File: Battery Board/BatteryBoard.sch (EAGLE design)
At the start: 34 parts, among them IC1 TPS63060DSCT, J0 1725656, J1 1725669, J2 UJ2-MIBH2-4-SMT-TR, J3 MPTC-02-16-02-6.30-XX-X-V, J4 JSTPH2, J5 MPTC-02-04-02-6.30-XX-X-V-LC, Q1 IAUC60N04S6L030HATMA1, U0 STM32L031K4U6, U1 MCP73831T-2ATI_OT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

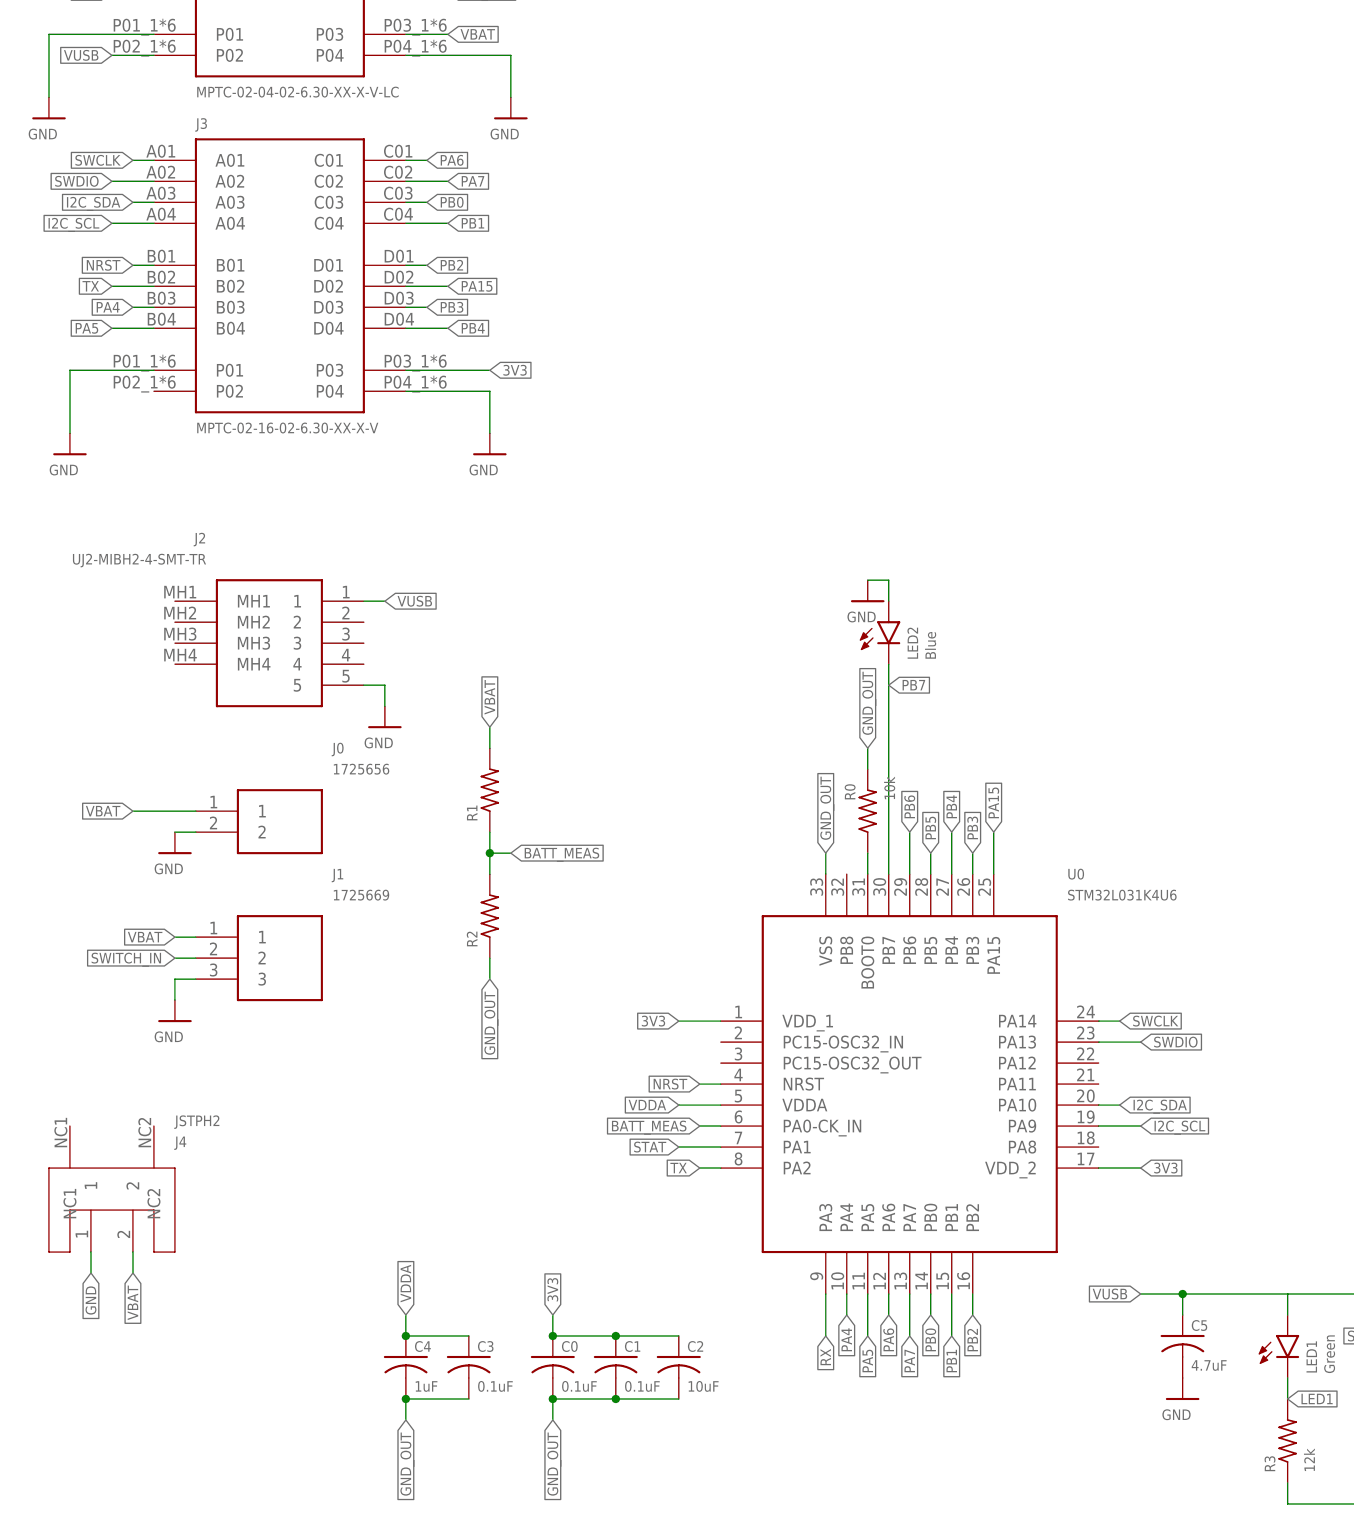
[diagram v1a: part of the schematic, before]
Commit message: Routed everything besides the pinheaders
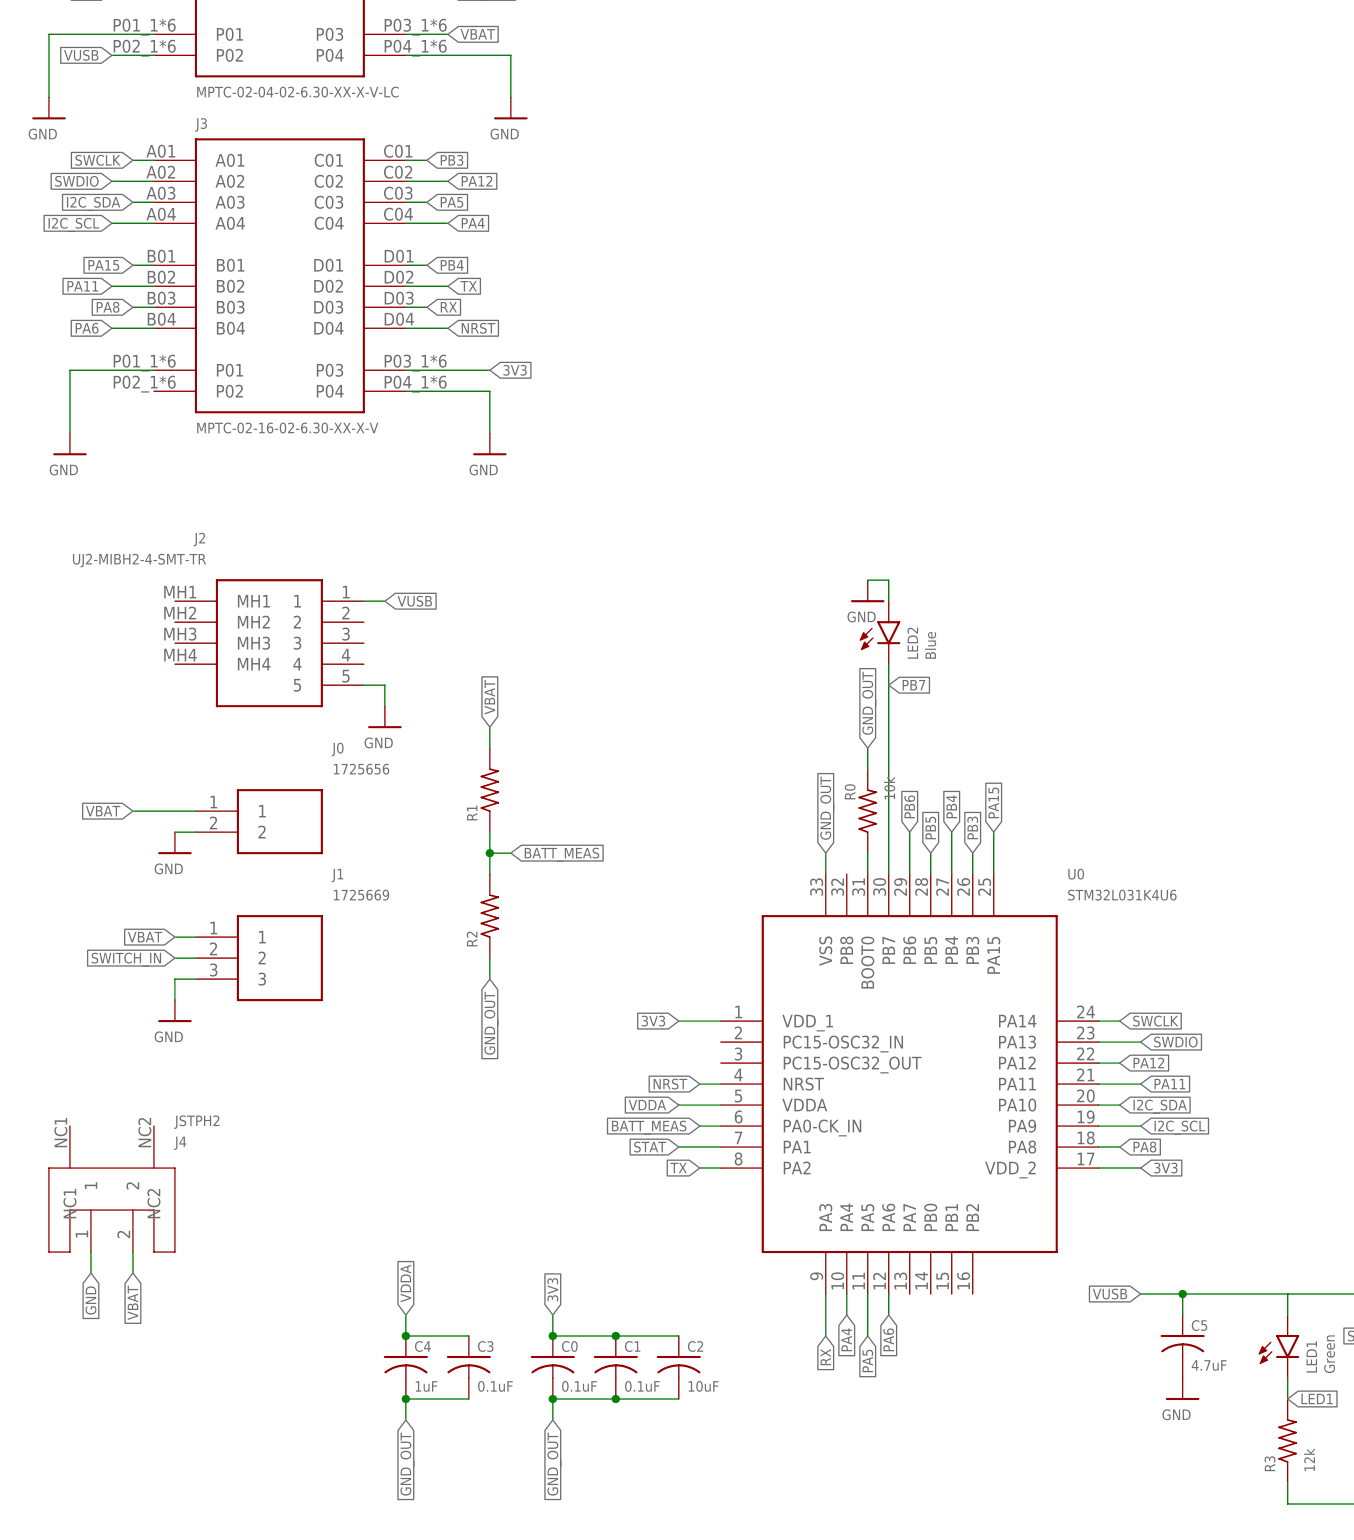
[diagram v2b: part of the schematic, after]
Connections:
- removed net PA7: J3.C02, U0.PA7
- removed net PB0: J3.C03, U0.PB0
- removed net PB1: J3.C04, U0.PB1
- removed net PB2: J3.D01, U0.PB2
- new net PA11: J3.B02, U0.PA11
- new net PA12: J3.C02, U0.PA12
- new net PA8: J3.B03, U0.PA8
- net NRST: now also J3.D04; no longer J3.B01
- net PA15: now also J3.B01; no longer J3.D02
- net PA4: now also J3.C04; no longer J3.B03
- net PA5: now also J3.C03; no longer J3.B04
- net PA6: now also J3.B04; no longer J3.C01
- net PB3: now also J3.C01; no longer J3.D03
- net PB4: now also J3.D01; no longer J3.D04
- net RX: now also J3.D03
- net TX: now also J3.D02; no longer J3.B02
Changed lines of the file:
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@@
 </segment>
 <segment>
-<pinref part="J3" gate="G$1" pin="B02"/>
-<wire x1="-53.34" y1="139.7" x2="-58.42" y2="139.7" width="0.1524" layer="91"/>
-<label x="-58.42" y="139.7" size="1.27" layer="95" rot="R180" xref="yes"/>
+<pinref part="J3" gate="G$1" pin="D02"/>
+<wire x1="-22.86" y1="139.7" x2="-17.78" y2="139.7" width="0.1524" layer="91"/>
+<label x="-17.78" y="139.7" size="1.27" layer="95" xref="yes"/>
 </segment>
 </net>
@@
 <label x="27.94" y="12.7" size="1.27" layer="95" rot="R270" xref="yes"/>
 </segment>
+<segment>
+<pinref part="J3" gate="G$1" pin="D03"/>
+<wire x1="-22.86" y1="137.16" x2="-20.32" y2="137.16" width="0.1524" layer="91"/>
+<label x="-20.32" y="137.16" size="1.27" layer="95" xref="yes"/>
+</segment>
 </net>
 <net name="NRST" class="0">
@@
 </segment>
 <segment>
-<pinref part="J3" gate="G$1" pin="B01"/>
-<wire x1="-53.34" y1="142.24" x2="-55.88" y2="142.24" width="0.1524" layer="91"/>
-<label x="-55.88" y="142.24" size="1.27" layer="95" rot="R180" xref="yes"/>
+<pinref part="J3" gate="G$1" pin="D04"/>
+<wire x1="-22.86" y1="134.62" x2="-17.78" y2="134.62" width="0.1524" layer="91"/>
+<label x="-17.78" y="134.62" size="1.27" layer="95" xref="yes"/>
 </segment>
 </net>
@@
 </segment>
 <segment>
-<pinref part="J3" gate="G$1" pin="D04"/>
-<wire x1="-22.86" y1="134.62" x2="-17.78" y2="134.62" width="0.1524" layer="91"/>
-<label x="-17.78" y="134.62" size="1.27" layer="95" xref="yes"/>
+<pinref part="J3" gate="G$1" pin="D01"/>
+<wire x1="-22.86" y1="142.24" x2="-20.32" y2="142.24" width="0.1524" layer="91"/>
+<label x="-20.32" y="142.24" size="1.27" layer="95" xref="yes"/>
 </segment>
 </net>
@@
 </segment>
 <segment>
-<pinref part="J3" gate="G$1" pin="D03"/>
-<wire x1="-22.86" y1="137.16" x2="-20.32" y2="137.16" width="0.1524" layer="91"/>
-<label x="-20.32" y="137.16" size="1.27" layer="95" xref="yes"/>
-</segment>
-</net>
-<net name="PB2" class="0">
-<segment>
-<pinref part="U0" gate="G$1" pin="PB2"/>
-<wire x1="45.72" y1="17.78" x2="45.72" y2="15.24" width="0.1524" layer="91"/>
-<label x="45.72" y="15.24" size="1.27" layer="95" rot="R270" xref="yes"/>
-</segment>
-<segment>
-<pinref part="J3" gate="G$1" pin="D01"/>
-<wire x1="-22.86" y1="142.24" x2="-20.32" y2="142.24" width="0.1524" layer="91"/>
-<label x="-20.32" y="142.24" size="1.27" layer="95" xref="yes"/>
-</segment>
-</net>
-<net name="PB1" class="0">
-<segment>
-<pinref part="U0" gate="G$1" pin="PB1"/>
-<wire x1="43.18" y1="17.78" x2="43.18" y2="12.7" width="0.1524" layer="91"/>
-<label x="43.18" y="12.7" size="1.27" layer="95" rot="R270" xref="yes"/>
+<pinref part="J3" gate="G$1" pin="C01"/>
+<wire x1="-22.86" y1="154.94" x2="-20.32" y2="154.94" width="0.1524" layer="91"/>
+<label x="-20.32" y="154.94" size="1.27" layer="95" xref="yes"/>
+</segment>
+</net>
+<net name="PA6" class="0">
+<segment>
+<pinref part="U0" gate="G$1" pin="PA6"/>
+<wire x1="35.56" y1="17.78" x2="35.56" y2="15.24" width="0.1524" layer="91"/>
+<label x="35.56" y="15.24" size="1.27" layer="95" rot="R270" xref="yes"/>
+</segment>
+<segment>
+<pinref part="J3" gate="G$1" pin="B04"/>
+<wire x1="-53.34" y1="134.62" x2="-58.42" y2="134.62" width="0.1524" layer="91"/>
+<label x="-58.42" y="134.62" size="1.27" layer="95" rot="R180" xref="yes"/>
+</segment>
+</net>
+<net name="PA5" class="0">
+<segment>
+<pinref part="U0" gate="G$1" pin="PA5"/>
+<wire x1="33.02" y1="17.78" x2="33.02" y2="12.7" width="0.1524" layer="91"/>
+<label x="33.02" y="12.7" size="1.27" layer="95" rot="R270" xref="yes"/>
+</segment>
+<segment>
+<pinref part="J3" gate="G$1" pin="C03"/>
+<wire x1="-22.86" y1="149.86" x2="-20.32" y2="149.86" width="0.1524" layer="91"/>
+<label x="-20.32" y="149.86" size="1.27" layer="95" xref="yes"/>
+</segment>
+</net>
+<net name="PA4" class="0">
+<segment>
+<pinref part="U0" gate="G$1" pin="PA4"/>
+<wire x1="30.48" y1="17.78" x2="30.48" y2="15.24" width="0.1524" layer="91"/>
+<label x="30.48" y="15.24" size="1.27" layer="95" rot="R270" xref="yes"/>
 </segment>
 <segment>
@@
 </segment>
 </net>
-<net name="PB0" class="0">
-<segment>
-<pinref part="U0" gate="G$1" pin="PB0"/>
-<wire x1="40.64" y1="17.78" x2="40.64" y2="15.24" width="0.1524" layer="91"/>
-<label x="40.64" y="15.24" size="1.27" layer="95" rot="R270" xref="yes"/>
-</segment>
-<segment>
-<pinref part="J3" gate="G$1" pin="C03"/>
-<wire x1="-22.86" y1="149.86" x2="-20.32" y2="149.86" width="0.1524" layer="91"/>
-<label x="-20.32" y="149.86" size="1.27" layer="95" xref="yes"/>
-</segment>
-</net>
-<net name="PA7" class="0">
-<segment>
-<pinref part="U0" gate="G$1" pin="PA7"/>
-<wire x1="38.1" y1="17.78" x2="38.1" y2="12.7" width="0.1524" layer="91"/>
-<label x="38.1" y="12.7" size="1.27" layer="95" rot="R270" xref="yes"/>
+<net name="PA15" class="0">
+<segment>
+<pinref part="U0" gate="G$1" pin="PA15"/>
+<wire x1="48.26" y1="68.58" x2="48.26" y2="73.66" width="0.1524" layer="91"/>
+<label x="48.26" y="73.66" size="1.27" layer="95" rot="R90" xref="yes"/>
+</segment>
+<segment>
+<pinref part="J3" gate="G$1" pin="B01"/>
+<wire x1="-53.34" y1="142.24" x2="-55.88" y2="142.24" width="0.1524" layer="91"/>
+<label x="-55.88" y="142.24" size="1.27" layer="95" rot="R180" xref="yes"/>
+</segment>
+</net>
+<net name="PA8" class="0">
+<segment>
+<pinref part="U0" gate="G$1" pin="PA8"/>
+<wire x1="60.96" y1="35.56" x2="63.5" y2="35.56" width="0.1524" layer="91"/>
+<label x="63.5" y="35.56" size="1.27" layer="95" xref="yes"/>
+</segment>
+<segment>
+<pinref part="J3" gate="G$1" pin="B03"/>
+<wire x1="-53.34" y1="137.16" x2="-55.88" y2="137.16" width="0.1524" layer="91"/>
+<label x="-55.88" y="137.16" size="1.27" layer="95" rot="R180" xref="yes"/>
+</segment>
+</net>
+<net name="PA11" class="0">
+<segment>
+<pinref part="U0" gate="G$1" pin="PA11"/>
+<wire x1="60.96" y1="43.18" x2="66.04" y2="43.18" width="0.1524" layer="91"/>
+<label x="66.04" y="43.18" size="1.27" layer="95" xref="yes"/>
+</segment>
+<segment>
+<pinref part="J3" gate="G$1" pin="B02"/>
+<wire x1="-53.34" y1="139.7" x2="-58.42" y2="139.7" width="0.1524" layer="91"/>
+<label x="-58.42" y="139.7" size="1.27" layer="95" rot="R180" xref="yes"/>
+</segment>
+</net>
+<net name="PA12" class="0">
+<segment>
+<pinref part="U0" gate="G$1" pin="PA12"/>
+<wire x1="60.96" y1="45.72" x2="63.5" y2="45.72" width="0.1524" layer="91"/>
+<label x="63.5" y="45.72" size="1.27" layer="95" xref="yes"/>
 </segment>
 <segment>
@@
 </segment>
 </net>
-<net name="PA6" class="0">
-<segment>
-<pinref part="U0" gate="G$1" pin="PA6"/>
-<wire x1="35.56" y1="17.78" x2="35.56" y2="15.24" width="0.1524" layer="91"/>
-<label x="35.56" y="15.24" size="1.27" layer="95" rot="R270" xref="yes"/>
-</segment>
-<segment>
-<pinref part="J3" gate="G$1" pin="C01"/>
-<wire x1="-22.86" y1="154.94" x2="-20.32" y2="154.94" width="0.1524" layer="91"/>
-<label x="-20.32" y="154.94" size="1.27" layer="95" xref="yes"/>
-</segment>
-</net>
-<net name="PA5" class="0">
-<segment>
-<pinref part="U0" gate="G$1" pin="PA5"/>
-<wire x1="33.02" y1="17.78" x2="33.02" y2="12.7" width="0.1524" layer="91"/>
-<label x="33.02" y="12.7" size="1.27" layer="95" rot="R270" xref="yes"/>
-</segment>
-<segment>
-<pinref part="J3" gate="G$1" pin="B04"/>
-<wire x1="-53.34" y1="134.62" x2="-58.42" y2="134.62" width="0.1524" layer="91"/>
-<label x="-58.42" y="134.62" size="1.27" layer="95" rot="R180" xref="yes"/>
-</segment>
-</net>
-<net name="PA4" class="0">
-<segment>
-<pinref part="U0" gate="G$1" pin="PA4"/>
-<wire x1="30.48" y1="17.78" x2="30.48" y2="15.24" width="0.1524" layer="91"/>
-<label x="30.48" y="15.24" size="1.27" layer="95" rot="R270" xref="yes"/>
-</segment>
-<segment>
-<pinref part="J3" gate="G$1" pin="B03"/>
-<wire x1="-53.34" y1="137.16" x2="-55.88" y2="137.16" width="0.1524" layer="91"/>
-<label x="-55.88" y="137.16" size="1.27" layer="95" rot="R180" xref="yes"/>
-</segment>
-</net>
-<net name="PA15" class="0">
-<segment>
-<pinref part="U0" gate="G$1" pin="PA15"/>
-<wire x1="48.26" y1="68.58" x2="48.26" y2="73.66" width="0.1524" layer="91"/>
-<label x="48.26" y="73.66" size="1.27" layer="95" rot="R90" xref="yes"/>
-</segment>
-<segment>
-<pinref part="J3" gate="G$1" pin="D02"/>
-<wire x1="-22.86" y1="139.7" x2="-17.78" y2="139.7" width="0.1524" layer="91"/>
-<label x="-17.78" y="139.7" size="1.27" layer="95" xref="yes"/>
-</segment>
-</net>

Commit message: New transistor design started
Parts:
- added Q2: MMBTA56LT1G, transistor:BC807-16-PNP-SOT23-BEC
- added R10: 1M, rcl:R-US_R0805
- added R8, R9: 10k, rcl:R-US_R0805
- Q1: value IAUC60N04S6L030HATMA1 -> MMBTA56LT1G; device MarkParts:IAUC60N04S6L030HATMA1 -> transistor:BC807-16-PNP-SOT23-BEC
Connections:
- removed net GND_OUT: C0.2, C1.2, C2.2, C3.2, C4.2, Q1.BATTERY, Q1.BATTERY_2, R0.2, R2.1, U0.VSS
- new net EN: IC1.EN, Q1.E, Q2.E, R10.1
- new net N$2: Q1.B, R8.1
- new net N$4: Q2.B, R9.1
- net GND: now also C0.2, C1.2, C2.2, C3.2, C4.2, Q1.C, Q2.C, R0.2, R2.1, U0.VSS; no longer Q1.GND, Q1.GND_2
- net PROTECTION_NRST: now also R8.2; no longer Q1.G_2
- net SWITCH_IN: now also R9.2; no longer Q1.G
- net VBAT: now also R10.2; no longer IC1.EN

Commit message: Touch up before final review
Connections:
- net GND: now also IC1.EP/PGND_1, IC1.EP/PGND_2, IC1.EP/PGND_3, IC1.EP/PGND_4, IC1.EP/PGND_5, IC1.EP/PGND_6, IC1.EP/PGND_7, IC1.EP/PGND_8
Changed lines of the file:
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@@
 <drawing>
 <settings>
-<setting alwaysvectorfont="no"/>
+<setting alwaysvectorfont="yes"/>
 <setting verticaltext="up"/>
 </settings>
@@
 <label x="-12.7" y="55.88" size="1.27" layer="95" rot="R270" xref="yes"/>
 </segment>
+<segment>
+<pinref part="IC1" gate="G$1" pin="EP/PGND_4"/>
+<pinref part="IC1" gate="G$1" pin="EP/PGND_3"/>
+<wire x1="203.2" y1="25.4" x2="203.2" y2="27.94" width="0.1524" layer="91"/>
+<pinref part="IC1" gate="G$1" pin="EP/PGND_2"/>
+<wire x1="203.2" y1="27.94" x2="203.2" y2="30.48" width="0.1524" layer="91"/>
+<junction x="203.2" y="27.94"/>
+<pinref part="IC1" gate="G$1" pin="EP/PGND_1"/>
+<wire x1="203.2" y1="30.48" x2="203.2" y2="33.02" width="0.1524" layer="91"/>
+<junction x="203.2" y="30.48"/>
+</segment>
+<segment>
+<pinref part="IC1" gate="G$1" pin="EP/PGND_8"/>
+<pinref part="IC1" gate="G$1" pin="EP/PGND_7"/>
+<wire x1="243.84" y1="33.02" x2="243.84" y2="30.48" width="0.1524" layer="91"/>
+<pinref part="IC1" gate="G$1" pin="EP/PGND_6"/>
+<wire x1="243.84" y1="30.48" x2="243.84" y2="27.94" width="0.1524" layer="91"/>
+<junction x="243.84" y="30.48"/>
+<pinref part="IC1" gate="G$1" pin="EP/PGND_5"/>
+<wire x1="243.84" y1="27.94" x2="243.84" y2="25.4" width="0.1524" layer="91"/>
+<junction x="243.84" y="27.94"/>
+</segment>
 </net>

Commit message: Routed draft
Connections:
- net I2C_SCL: now also J5.C01; no longer J5.D01
- net I2C_SDA: now also J5.D01; no longer J5.C01
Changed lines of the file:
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@@
-</segment>
-<segment>
-<pinref part="J5" gate="G$1" pin="C01"/>
-<wire x1="-22.86" y1="180.34" x2="-17.78" y2="180.34" width="0.1524" layer="91"/>
-<label x="-17.78" y="180.34" size="1.27" layer="95" xref="yes"/>
 </segment>
 <segment>
@@
 <wire x1="-53.34" y1="149.86" x2="-55.88" y2="149.86" width="0.1524" layer="91"/>
 <label x="-55.88" y="149.86" size="1.27" layer="95" rot="R180" xref="yes"/>
+</segment>
+<segment>
+<pinref part="J5" gate="G$1" pin="D01"/>
+<wire x1="-22.86" y1="175.26" x2="-17.78" y2="175.26" width="0.1524" layer="91"/>
+<label x="-17.78" y="175.26" size="1.27" layer="95" xref="yes"/>
 </segment>
 </net>
@@
 </segment>
 <segment>
-<pinref part="J5" gate="G$1" pin="D01"/>
-<wire x1="-22.86" y1="175.26" x2="-17.78" y2="175.26" width="0.1524" layer="91"/>
-<label x="-17.78" y="175.26" size="1.27" layer="95" xref="yes"/>
-</segment>
-<segment>
 <pinref part="J3" gate="G$1" pin="A04"/>
 <wire x1="-53.34" y1="147.32" x2="-58.42" y2="147.32" width="0.1524" layer="91"/>
 <label x="-58.42" y="147.32" size="1.27" layer="95" rot="R180" xref="yes"/>
 </segment>
+<segment>
+<pinref part="J5" gate="G$1" pin="C01"/>
+<wire x1="-22.86" y1="180.34" x2="-17.78" y2="180.34" width="0.1524" layer="91"/>
+<label x="-17.78" y="180.34" size="1.27" layer="95" xref="yes"/>
+</segment>
 </net>
